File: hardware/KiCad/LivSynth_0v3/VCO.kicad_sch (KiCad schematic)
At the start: 26 parts, among them J15 Jumper, J16 Jumper, J17 Jumper, Q11 2N3904, Q12 2N3904, Q14 2N3904, SW1 SW_SPDT, U2 TL074, U4 TL074

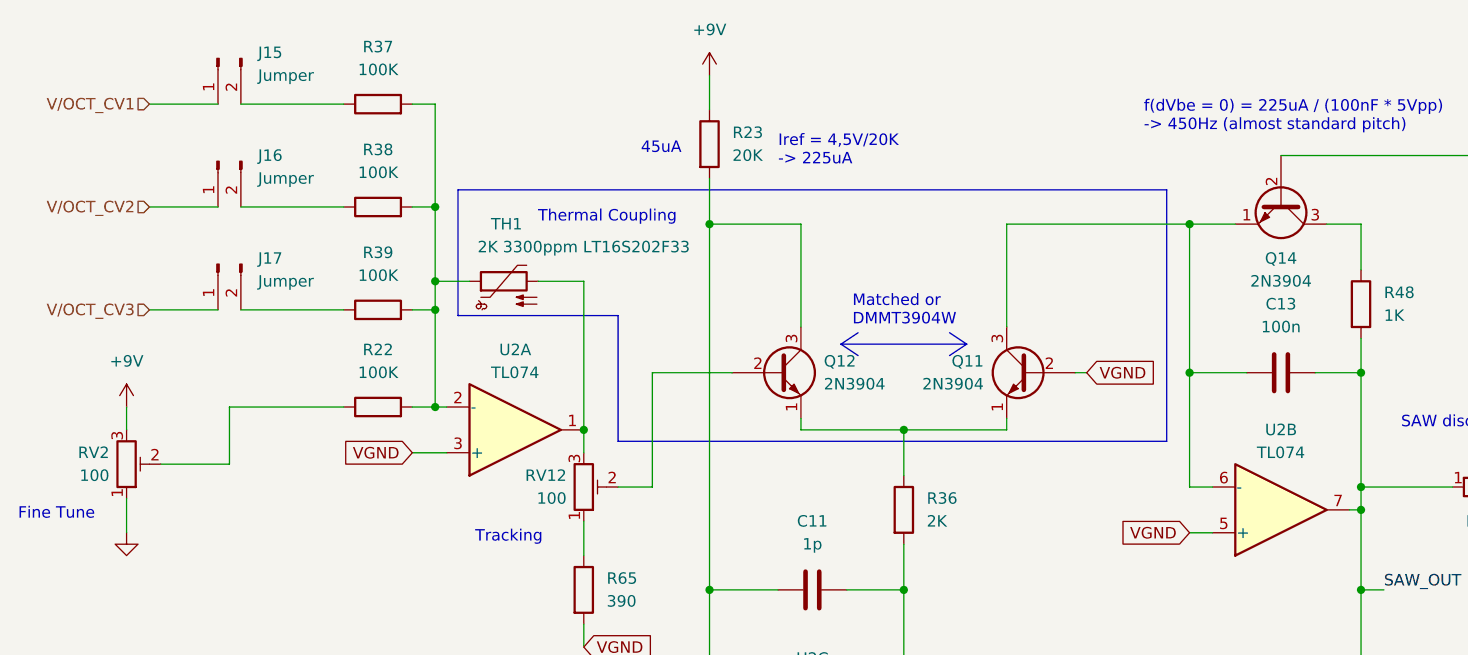
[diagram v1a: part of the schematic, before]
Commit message: RV11 = 100K update BOM RV2 = 100K C13 = 10n R23 = 470K
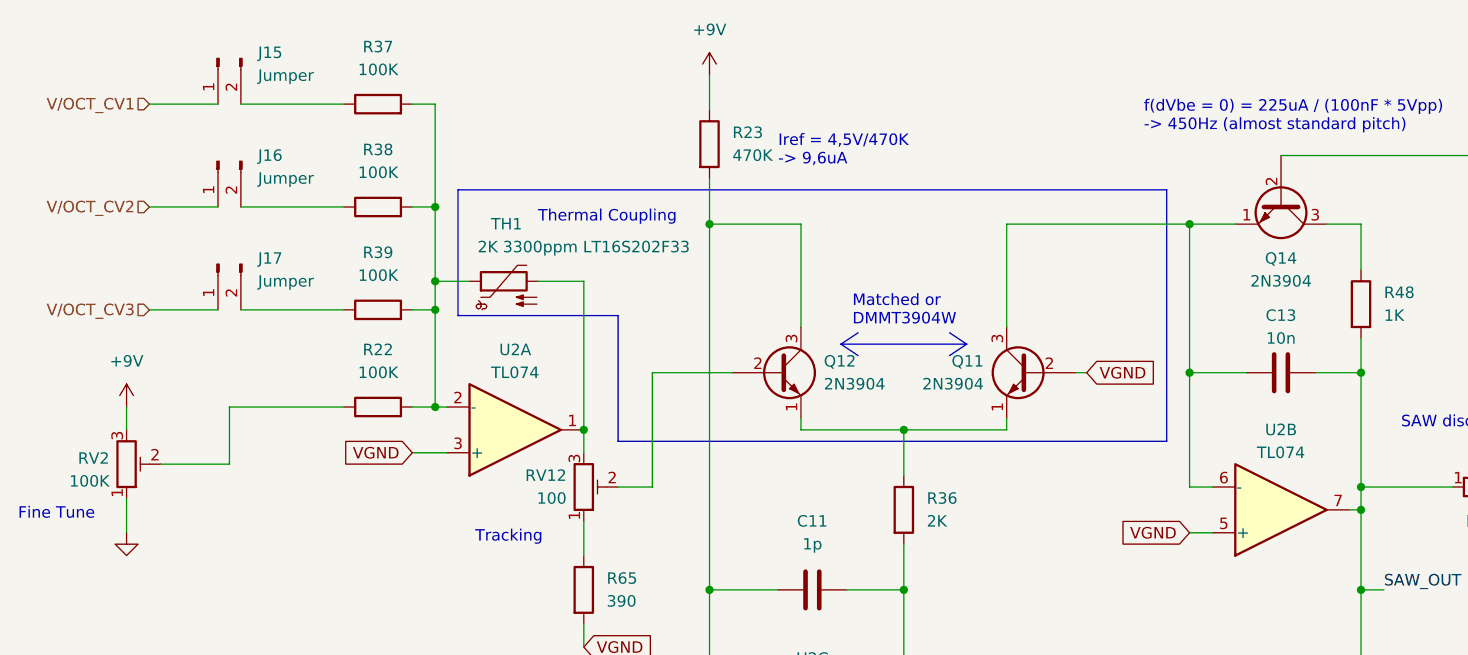
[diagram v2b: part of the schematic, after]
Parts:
- C13: value 100n -> 10n
- R23: value 20K -> 470K
- RV2: value 100 -> 100K
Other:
- note added: "Iref = 4,5V/470K -> 9,6uA"
- note removed: "45uA"
- note removed: "Iref = 4,5V/20K -> 225uA"
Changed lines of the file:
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@@
-    (effects (font (size 1.27 1.27)) (justify left bottom))
-  )
-  (text "45uA" (at 102.235 45.72 0)
     (effects (font (size 1.27 1.27)) (justify left bottom))
   )
@@
     (effects (font (size 1.27 1.27)) (justify left bottom))
   )
-  (text "Iref = 4,5V/20K\n-> 225uA" (at 117.475 46.99 0)
+  (text "Iref = 4,5V/470K\n-> 9,6uA" (at 117.475 46.99 0)
     (effects (font (size 1.27 1.27)) (justify left bottom))
   )
@@
   (symbol (lib_id "Device:C") (at 173.355 69.85 90) (unit 1)
     (in_bom yes) (on_board yes) (dnp no) (fields_autoplaced)
-    (property "Reference" "C13" (at 173.355 62.23 90)
-      (effects (font (size 1.27 1.27)))
-    )
-    (property "Value" "100n" (at 173.355 64.77 90)
+    (property "Reference" "C13" (at 173.355 63.5 90)
+      (effects (font (size 1.27 1.27)))
+    )
+    (property "Value" "10n" (at 173.355 66.04 90)
       (effects (font (size 1.27 1.27)))
     )
@@
   (symbol (lib_id "Device:R_Potentiometer_Trim") (at 45.085 80.01 0) (mirror x) (unit 1)
     (in_bom yes) (on_board yes) (dnp no) (fields_autoplaced)
-    (property "Reference" "RV2" (at 43.18 78.7399 0)
-      (effects (font (size 1.27 1.27)) (justify right))
-    )
-    (property "Value" "100" (at 43.18 81.2799 0)
+    (property "Reference" "RV2" (at 43.18 79.375 0)
+      (effects (font (size 1.27 1.27)) (justify right))
+    )
+    (property "Value" "100K" (at 43.18 81.915 0)
       (effects (font (size 1.27 1.27)) (justify right))
     )
@@
       (effects (font (size 1.27 1.27)) (justify left))
     )
-    (property "Value" "20K" (at 112.395 45.72 0)
-      (effects (font (size 1.27 1.27)) (justify left))
-    )
+    (property "Value" "470K" (at 112.395 45.72 0)
+      (effects (font (size 1.27 1.27)) (justify left))
+    )
